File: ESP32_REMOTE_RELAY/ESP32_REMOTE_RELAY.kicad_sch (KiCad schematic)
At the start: 13 parts, among them J1 AC_MAINS, J2 Bulvack LM2596, J3 RC Snubber Mod., J4 RC Snubber Mod., J5 Bulvack LM2596, K1 Teylen Robot Optocoupler 3V3 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, K2 Teylen Robot Optocoupler 3V3 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, U1 ESP32-WROOM-32

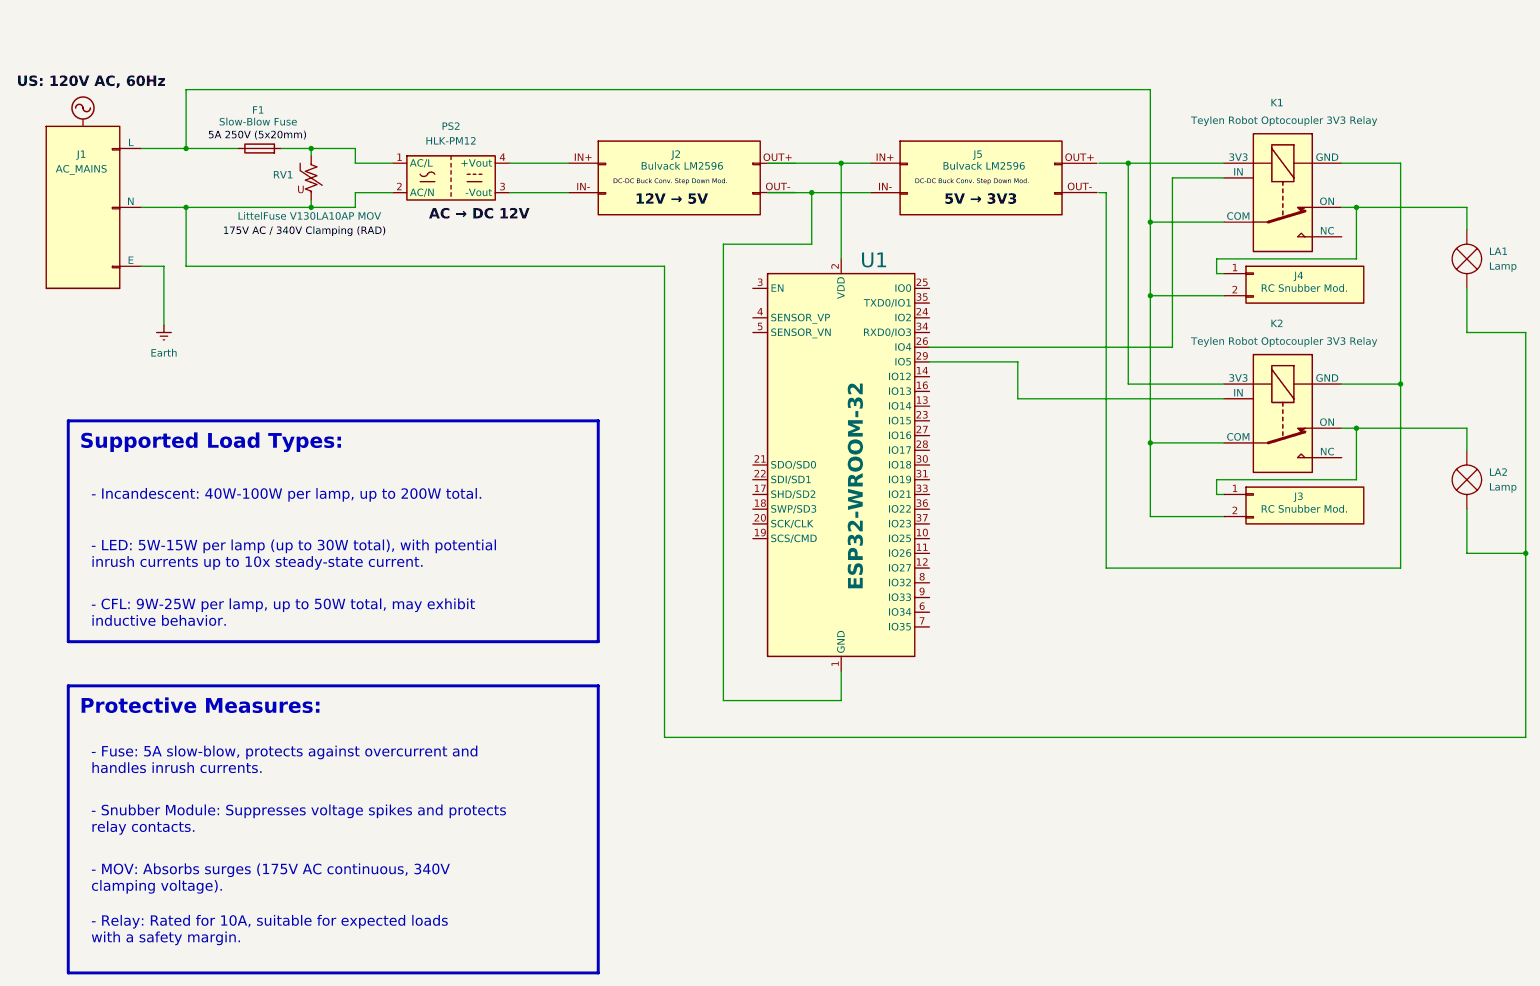
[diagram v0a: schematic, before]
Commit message: Replaced HLK-PM12 with HLK-PM03 and removed both step-down bucks; now powering MCU via 3V3 pin instead of USB. Also added decoupling and bulk capacitors.
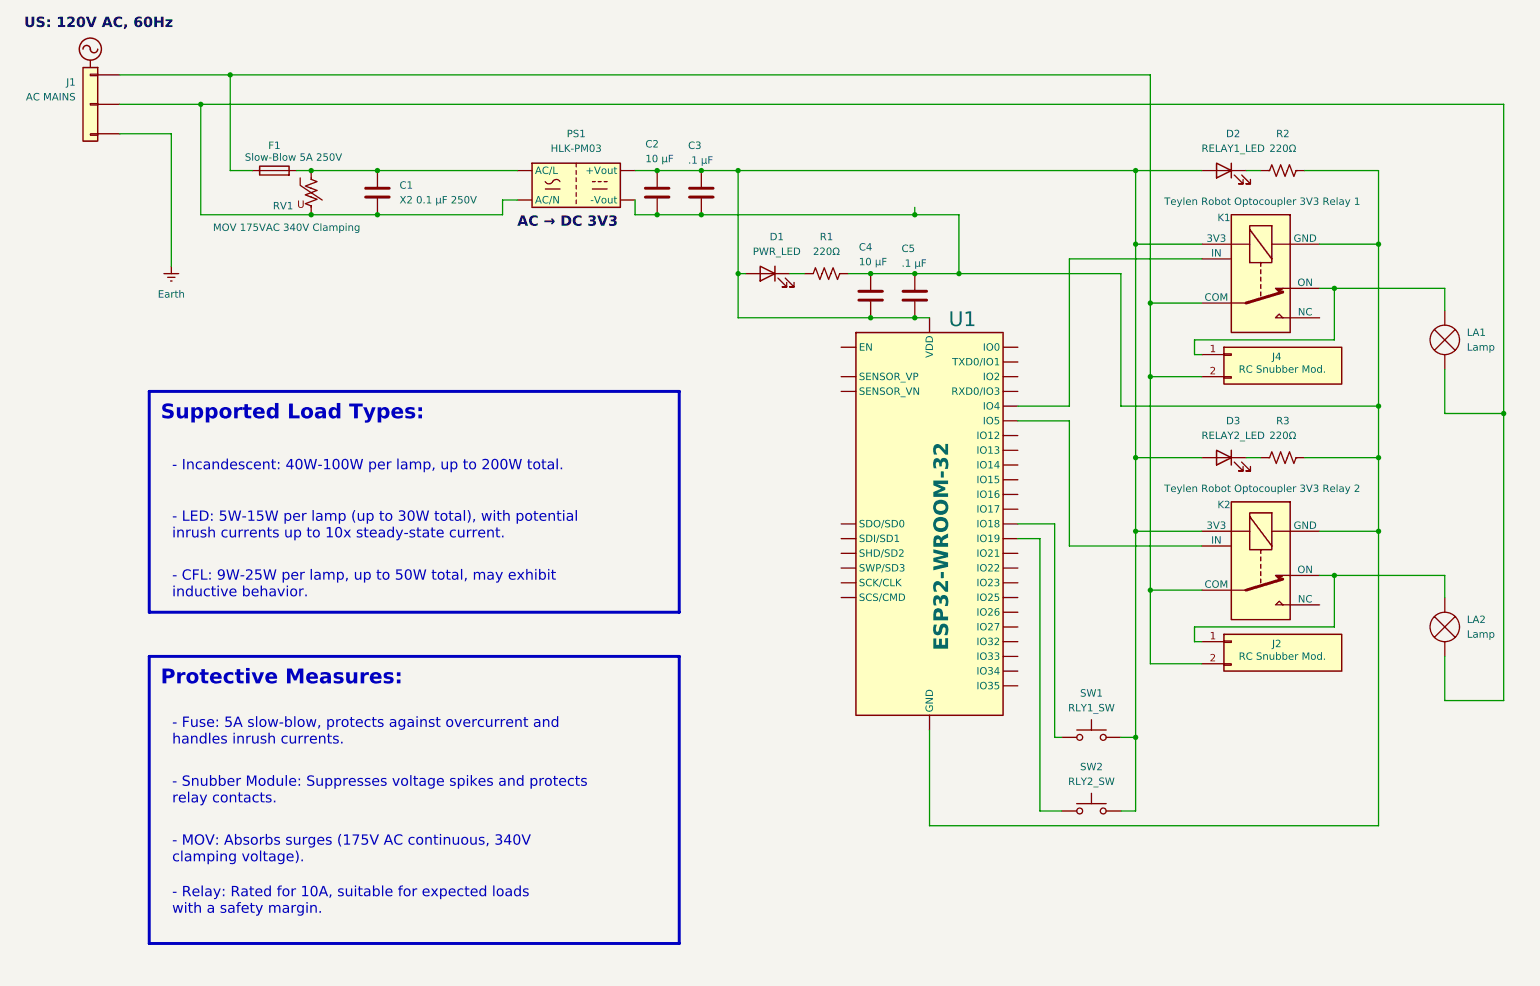
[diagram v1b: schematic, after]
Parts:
- removed J2, J5: Bulvack LM2596, symbol Connector_Generic:Conn_02x02_Counter_Clockwise
- removed J3: RC Snubber Mod., symbol Connector_Generic:Conn_01x02
- removed PS2: HLK-PM12, Converter_ACDC:Converter_ACDC_Hi-Link_HLK-PMxx, symbol Converter_ACDC:HLK-PM12
- added C1: X2 0.1 µF 250V, symbol Device:C
- added C2, C4: 10 µF, symbol Device:C
- added C3, C5: .1 µF, symbol Device:C
- added D1: PWR_LED, symbol Device:LED
- added D2: RELAY1_LED, symbol Device:LED
- added D3: RELAY2_LED, symbol Device:LED
- added J2: RC Snubber Mod., symbol Connector_Generic:Conn_01x02
- added PS1: HLK-PM03, Converter_ACDC:Converter_ACDC_Hi-Link_HLK-PMxx, symbol Converter_ACDC:HLK-PM03
- added R1, R2, R3: 220Ω, symbol Device:R_US
- added SW1: RLY1_SW, symbol Switch:SW_Push
- added SW2: RLY2_SW, symbol Switch:SW_Push
- F1: value Slow-Blow Fuse -> Slow-Blow 5A 250V
- J1: value AC_MAINS -> AC MAINS
- K1: value Teylen Robot Optocoupler 3V3 Relay -> Teylen Robot Optocoupler 3V3 Relay 1
- K2: value Teylen Robot Optocoupler 3V3 Relay -> Teylen Robot Optocoupler 3V3 Relay 2
- RV1: value LittelFuse V130LA10AP MOV -> MOV 175VAC 340V Clamping
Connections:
- net at K2.2 (ON), LA2.2 (+): now also J2.1 (Pin_1)
- net at K1.3 (3V3), K2.3 (3V3): now also U1.2 (VDD), C2.1, C3.1, C4.2, C5.2, D1.2 (A), D2.2 (A), D3.2 (A), PS1.4 (+Vout), SW1.2, SW2.2
- net at K1.5 (GND), K2.5 (GND): now also U1.1 (GND), U1.15 (GND), U1.38 (GND), U1.39 (GND), C2.2, C3.2, C4.1, C5.1, PS1.3 (-Vout), R1.2, R2.2, R3.2
- net at F1.1, J1.1 (L), J4.2 (Pin_2)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: now also J2.2 (Pin_2)
- net at F1.2, RV1.1: now also C1.1, PS1.1 (AC/L)
- net at J1.2 (N), LA1.1 (-), LA2.1 (-)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: now also C1.2, PS1.2 (AC/N)
- net at U1.30 (IO18): now also SW1.1
- net at U1.31 (IO19): now also SW2.1
- new net: D1.1 (K), R1.1
- new net: D2.1 (K), R2.1
- new net: D3.1 (K), R3.1
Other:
- moved on the sheet: F1, J4, K1, LA1, RV1
